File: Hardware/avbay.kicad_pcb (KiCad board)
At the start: 2 copper layers, 45.7 x 95.3 mm, 53 parts, among them P1 TERM_BLOCK_2.54MM_2POS, P2 CONN_6, P3 TERM_BLOCK_2.54MM_8POS, P4 TERM_BLOCK_2.54MM_5POS, P5 TERM_BLOCK_2.54MM_5POS, P6 TERM_BLOCK_2.54MM_2POS, P7 TERM_BLOCK_2.54MM_8POS, Q1 DMN2041LSD, Q2 BSS138DW, Q3 DMN2041LSD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

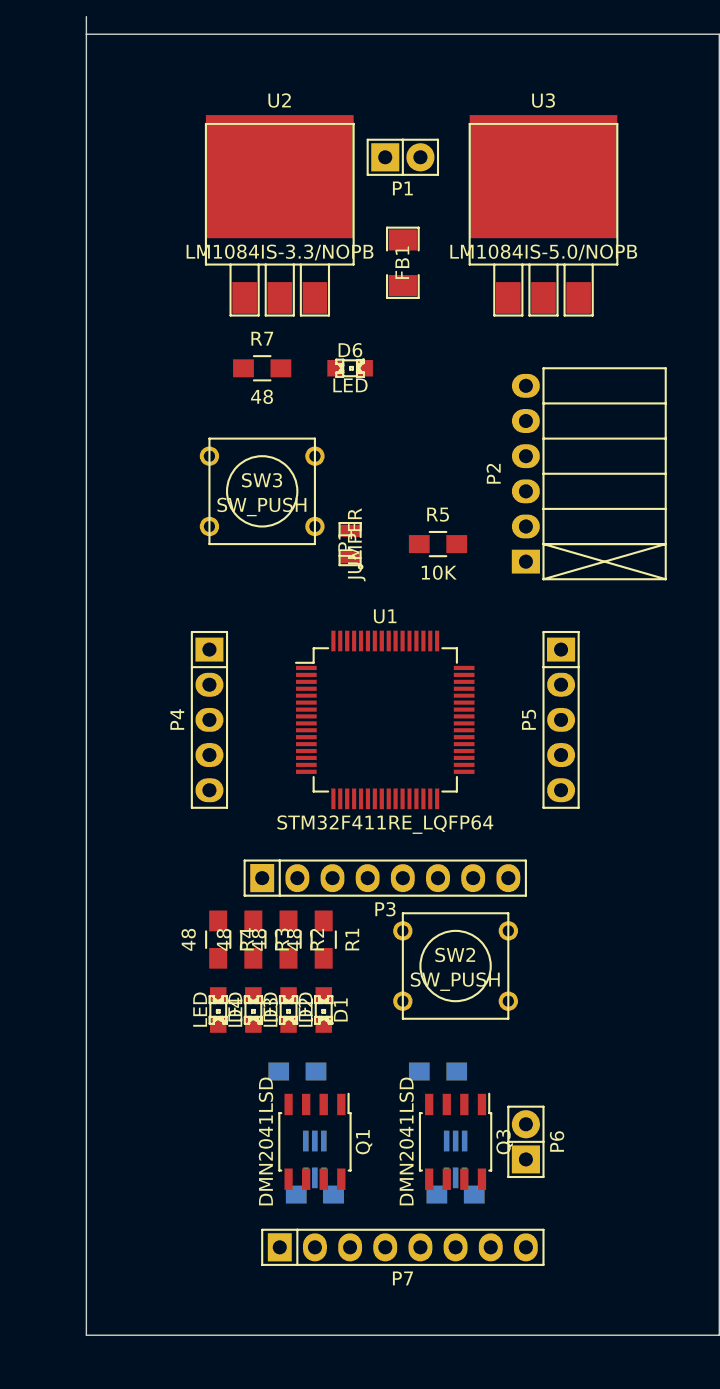
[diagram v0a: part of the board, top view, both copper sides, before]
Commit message: Roughed out PCB layout
Known issues:
- SW_PUSH holes too small. New footprint needed
- Sensor footprints are completely wrong.
- Regulator footprints might not be correct.

Tasks:
- Place passives according to schematic (especially
  with decoupling capacitors.
- Condense layout as much as possible for
  smallest board size
- Route board
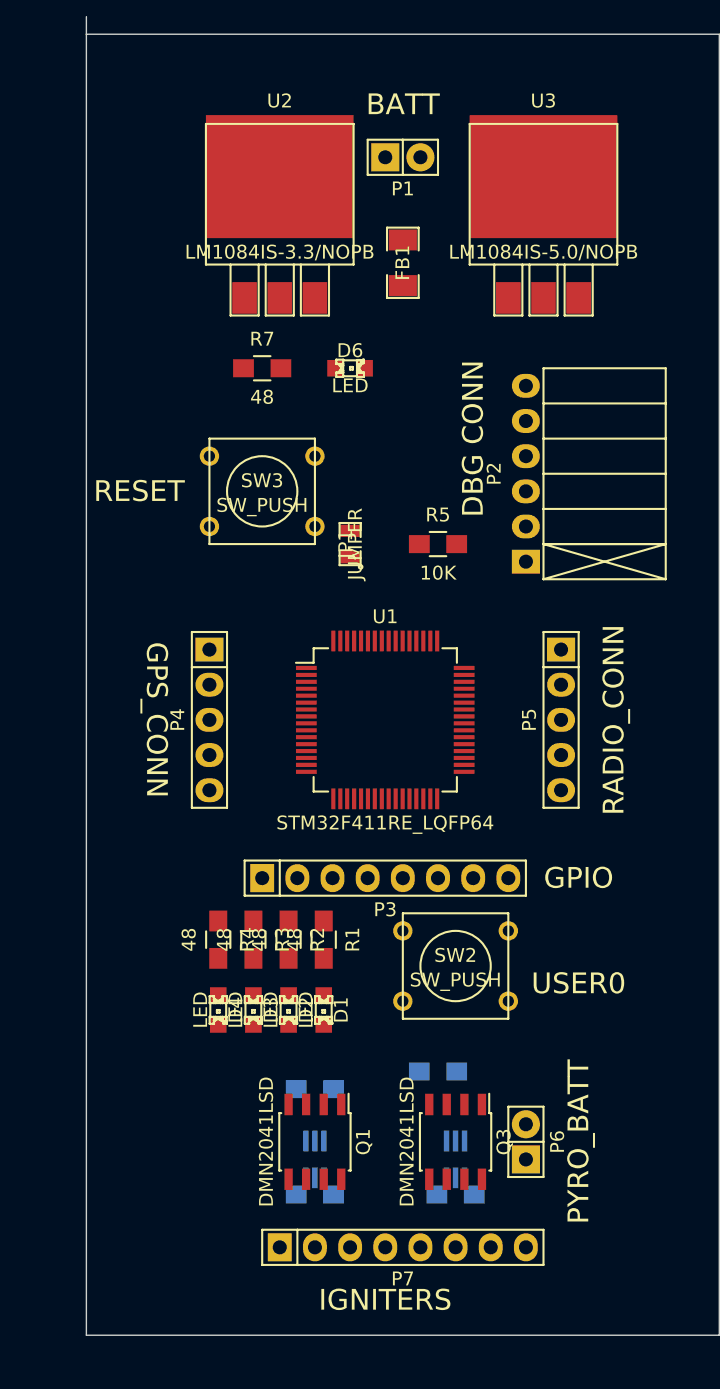
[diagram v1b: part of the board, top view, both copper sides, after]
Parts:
- moved R8 1.80 mm to (147.3, 114.3)
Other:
- board text added: "BATT"
- board text added: "DBG CONN"
- board text added: "GPIO"
- board text added: "GPS_CONN"
- board text added: "IGNITERS"
- board text added: "PYRO_BATT"
- board text added: "RADIO_CONN"
- board text added: "RESET"
- board text added: "USER0"
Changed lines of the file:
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@@
     (area 0 0 0 0)
     (thickness 1.6)
-    (drawings 5)
+    (drawings 14)
     (tracks 0)
     (zones 0)
@@
   )
   (module Resistors_SMD:R_0805_HandSoldering (layer B.Cu)
-    (at 146.05 113.03)
+    (at 147.32 114.3)
     (descr "Resistor SMD 0805, hand soldering")
     (tags "resistor 0805")
@@
     )
   )
+  (gr_text "DBG CONN" (at 158.75 67.31 90) (layer F.SilkS)
+    (effects (font (size 1.5 1.5) (thickness 0.3)))
+  )
+  (gr_text RESET (at 134.62 71.12) (layer F.SilkS)
+    (effects (font (size 1.5 1.5) (thickness 0.3)))
+  )
+  (gr_text BATT (at 153.67 43.18) (layer F.SilkS)
+    (effects (font (size 1.5 1.5) (thickness 0.3)))
+  )
+  (gr_text IGNITERS (at 152.4 129.54) (layer F.SilkS)
+    (effects (font (size 1.5 1.5) (thickness 0.3)))
+  )
+  (gr_text PYRO_BATT (at 166.37 118.11 90) (layer F.SilkS)
+    (effects (font (size 1.5 1.5) (thickness 0.3)))
+  )
+  (gr_text "USER0\n" (at 166.37 106.68) (layer F.SilkS)
+    (effects (font (size 1.5 1.5) (thickness 0.3)))
+  )
+  (gr_text GPIO (at 166.37 99.06) (layer F.SilkS)
+    (effects (font (size 1.5 1.5) (thickness 0.3)))
+  )
+  (gr_text GPS_CONN (at 135.89 87.63 270) (layer F.SilkS)
+    (effects (font (size 1.5 1.5) (thickness 0.3)))
+  )
+  (gr_text "RADIO_CONN\n" (at 168.91 87.63 90) (layer F.SilkS)
+    (effects (font (size 1.5 1.5) (thickness 0.3)))
+  )
   (gr_line (start 130.81 38.1) (end 130.81 36.83) (angle 90) (layer Edge.Cuts) (width 0.1))

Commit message: Began routing
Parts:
- C1, C10, C15, C16, C2, C3, C4, C6, C7, C8, C9, FB1, R6: moved to B.Cu
- U5: footprint Housings_SSOP:SSOP-16_4.4x5.2mm_Pitch0.65mm -> PQFN:PQFN50P300X300-16N-EXTENDED
- U6: footprint Housings_SSOP:SSOP-16_4.4x5.2mm_Pitch0.65mm -> PQFN:PQFN65P400X400-16N-EXTENDED
- moved C12 105.9 mm to (162.6, 62.1), turned to 180 degrees
- moved C16 102.0 mm to (156.2, 69.2)
- moved C13 101.9 mm to (160.0, 60.3), turned to 180 degrees
- moved C4 99.2 mm to (158.1, 60.3), turned to 90 degrees
- moved C15 97.8 mm to (156.2, 77.5)
- moved C3 93.0 mm to (154.9, 57.8), turned to 180 degrees
- moved C8 92.6 mm to (156.8, 93.3), turned to 180 degrees
- moved C14 91.6 mm to (142.2, 60.3), turned to 180 degrees
- moved C5 88.3 mm to (160.0, 95.9), turned to 180 degrees
- moved C9 87.2 mm to (158.1, 83.2), turned to 270 degrees
- moved C2 84.5 mm to (146.1, 63.5), turned to 180 degrees
- moved C11 79.7 mm to (147.3, 60.3)
- moved C7 77.4 mm to (146.1, 67.9)
- moved C1 76.8 mm to (146.1, 60.3), turned to 180 degrees
- moved U5 75.1 mm to (154.9, 61.0), turned to 90 degrees
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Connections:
- C1 pad 1: +3V3 -> 3V3
- FB1 pad 1: +3V3 -> 3V3
- P3 pad 5: +3V3 -> 3V3
- U1 pad 12: /MCU/VDDA -> GND
- U1 pad 13: GND -> /MCU/VDDA
- U1 pad 25: GND -> /MCU/BTN1
- U4 pad 4: +3V3 -> 3V3
- U4 pad 5: +3V3 -> 3V3
- U5 pad 13: +3V3 -> 3V3
- U5 pad 4: +3V3 -> 3V3
- U6 pad 1: +3V3 -> 3V3
- U6 pad 4: +3V3 -> 3V3
- U6 pad 5: +3V3 -> 3V3
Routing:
- net GND: track 0.00 -> 215.6 mm, vias 0 -> 9
- net 3V3: track 0.00 -> 199.1 mm, vias 0 -> 9
- net +5V: track 0.00 -> 95.9 mm
- net /MCU/SENSE1: track 0.00 -> 46.0 mm, vias 0 -> 3
- net /MCU/SENSE2: track 0.00 -> 45.9 mm, vias 0 -> 3
- net /MCU/TRIGGER2: track 0.00 -> 44.9 mm, vias 0 -> 2
- net /Sheet54375BB5/Vbatt: track 0.00 -> 43.3 mm, vias 0 -> 1
- net /MCU/TRIGGER1: track 0.00 -> 41.7 mm, vias 0 -> 2
- net Net-(P7-Pad1): track 0.00 -> 30.8 mm, vias 0 -> 1
- net /MCU/VDDA: track 0.00 -> 27.1 mm, vias 0 -> 3
- net /Pyro/V_PYRO: track 0.00 -> 25.2 mm
- net Net-(P7-Pad7): track 0.00 -> 23.0 mm, vias 0 -> 1
- net Net-(P7-Pad3): track 0.00 -> 23.0 mm
- net /Sensors/SDA: track 0.00 -> 18.0 mm, vias 0 -> 4
- net /MCU/LED0: track 0.00 -> 17.0 mm
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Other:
- net class Default: clearance 0.254 -> 0.1524; trace_width 0.254 -> 0.1524; via_dia 0.889 -> 0.71374; via_drill 0.635 -> 0.3302
- net class Power added: clearance 0.1524, trace_width 0.2032, via_dia 0.71374, via_drill 0.3302
- rule trace_clearance: 0.254 -> 0.1524
- rule trace_min: 0.254 -> 0.1524
- rule via_min_drill: 0.508 -> 0.3302
- rule via_min_size: 0.889 -> 0.71374

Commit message: Finished routing.
Board awaiting review
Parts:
- added 1pin: VAL**, Connect:1pin, F.Cu at (152.4, 53.3)
- P2: footprint Socket_Strips:Socket_Strip_Angled_1x06 -> Socket_Strips:Socket_Strip_Straight_1x06
- moved D6 4.32 mm to (152.4, 49.7)
- moved R7 3.43 mm to (152.4, 48.0)
- moved P2 0.13 mm to (160.5, 71.1)
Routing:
- net GND: track 215.6 -> 349.2 mm, vias 9 -> 18
- net /MCU/NRST: track 0.00 -> 51.9 mm, vias 0 -> 5
- net /MCU/SENSE3: track 0.00 -> 51.7 mm, vias 0 -> 5
- net /MCU/SENSE4: track 0.00 -> 36.6 mm, vias 0 -> 5
- net /MCU/USART_RX: track 0.00 -> 33.4 mm, vias 0 -> 7
- net /MCU/RADIO_RX: track 0.00 -> 32.8 mm, vias 0 -> 6
- net /MCU/TRIGGER4: track 0.00 -> 32.6 mm, vias 0 -> 4
- net /MCU/TRIGGER3: track 0.00 -> 32.5 mm, vias 0 -> 4
- net /MCU/VDDA: track 27.1 -> 56.3 mm, vias 3 -> 6
- net /MCU/JTDO-SWO: track 0.00 -> 25.0 mm, vias 0 -> 2
- net /MCU/RADIO_TX: track 0.00 -> 23.9 mm, vias 0 -> 3
- net /MCU/JTMS-SWDIO: track 0.00 -> 21.1 mm, vias 0 -> 2
- net 3V3: track 199.1 -> 220.0 mm
- net /Sensors/SDA: track 18.0 -> 36.4 mm, vias 4 -> 6
- net /Sensors/SCL: track 15.3 -> 33.1 mm, vias 2 -> 4
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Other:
- board size 45.7 x 95.3 mm -> 30.5 x 81.3 mm
- board text added: "+"
- board text added: "-"
- board text added: "DEBUG"
- board text added: "GPS"
- board text added: "RADIO"
- board text removed: "BATT"
- board text removed: "DBG CONN"
- board text removed: "GPIO"
- board text removed: "GPS_CONN"
- board text removed: "IGNITERS"
- board text removed: "PYRO_BATT"
- board text removed: "RADIO_CONN"
- board text removed: "USER0"

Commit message: Fixed footprints for tecminal blocks
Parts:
- P1, P6: value TERM_BLOCK_2.54MM_2POS -> (none); footprint Socket_Strips:Socket_Strip_Straight_1x02 -> Local:TERM_BLOCK_2
- P3: value TERM_BLOCK_2.54MM_8POS -> (none)
- P4, P5: value TERM_BLOCK_2.54MM_5POS -> (none); footprint Socket_Strips:Socket_Strip_Straight_1x05 -> Local:TERM_BLOCK_5
- P7: value TERM_BLOCK_2.54MM_8POS -> (none); footprint Socket_Strips:Socket_Strip_Straight_1x08 -> Local:TERM_BLOCK_8
- moved P7 8.89 mm to (143.5, 122.6), turned to 0 degrees
- moved P3 8.89 mm to (143.5, 99.1), turned to 0 degrees
- moved P4 5.08 mm to (141.0, 82.5), turned to 270 degrees
- moved P5 5.08 mm to (163.8, 82.5), turned to 270 degrees
- moved P1 1.27 mm to (151.1, 45.7), turned to 0 degrees
- moved P6 1.27 mm to (161.3, 116.8), turned to 90 degrees
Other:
- outline, holes or cut-outs redrawn

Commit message: Finished schematic work. Began footprints
Began assigning footprints for R2
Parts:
- removed 1pin: VAL**, Connect:1pin
- removed C11, C12, C13, C14: 10uF, Capacitors_SMD:C_0805_HandSoldering
- removed C15: .01uF, Capacitors_SMD:C_0805_HandSoldering
- removed C16: .47uF, Capacitors_SMD:C_0805_HandSoldering
- removed C3: .22uF, Capacitors_SMD:C_0805_HandSoldering
- removed C4: 4.6uF, Capacitors_SMD:C_0805_HandSoldering
- removed C7: 100nF, Capacitors_SMD:C_0805_HandSoldering
- removed D6: LED, LEDs:LED-0805
- removed P1: , Local:TERM_BLOCK_2
- removed R6: 10K, Resistors_SMD:R_0805_HandSoldering
- removed R7: 48, Resistors_SMD:R_0805_HandSoldering
- removed SW3: SW_PUSH, Discret:SW_PUSH_SMALL
- removed U2: LM1084IS-3.3/NOPB, SMD_Packages:DPAK-3
- removed U3: LM1084IS-5.0/NOPB, SMD_Packages:DPAK-3
- removed U4: MS5611, SON:SON125P500X300-8N
- removed U5: HMC5883L, PQFN:PQFN50P300X300-16N-EXTENDED
- removed U6: L3G4200D, PQFN:PQFN65P400X400-16N-EXTENDED
- added R12: 10K, Resistors_SMD:R_0805_HandSoldering, F.Cu at (140.2, 111.4)
- added R13: 10K, Resistors_SMD:R_0805_HandSoldering, F.Cu at (140.2, 113.9)
- added R14, R15: 10K, Resistors_SMD:R_0805_HandSoldering, F.Cu at (152.4, 134.5)
- P3, P7: value (none) -> TERM_BLOCK_2.54MM_8POS
- P4, P5: value (none) -> TERM_BLOCK_2.54MM_5POS
- P6: value (none) -> TERM_BLOCK_2.54MM_2POS
- moved P2 2.39 mm to (162.8, 70.4)
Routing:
- net GND: track 349.2 -> 229.8 mm, vias 18 -> 13
- net 3V3: track 220.0 -> 149.9 mm
- net /MCU/NRST: track 51.9 -> 0.00 mm, vias 5 -> 0
- net /Sheet54375BB5/Vbatt: track 44.9 -> 0.00 mm, vias 2 -> 0
- net +5V: track 96.5 -> 55.0 mm
- net /MCU/VDDA: track 56.3 -> 19.5 mm, vias 6 -> 3
- net /Sensors/SDA: track 36.4 -> 0.00 mm, vias 6 -> 0
- net /Sensors/SCL: track 33.1 -> 0.00 mm, vias 4 -> 0
- net /MCU/JTDO-SWO: track 25.0 -> 0.00 mm, vias 2 -> 0
- net /MCU/JTMS-SWDIO: track 21.1 -> 0.00 mm, vias 2 -> 0
- net Net-(C15-Pad1): track 14.1 -> 0.00 mm, vias 2 -> 0
- net /MCU/JTCK-SWCLK: track 9.16 -> 0.00 mm, vias 2 -> 0
- net /MCU/TRIGGER1: track 42.1 -> 35.7 mm, vias 2 -> 1
- net Net-(C3-Pad1): track 6.21 -> 0.00 mm, vias 2 -> 0
- net Net-(C16-Pad2): track 6.08 -> 0.00 mm
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
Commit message: Ready to begin laying out and routing
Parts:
- added ?: , Local:MOUNTING_HOLE_3mm, F.Cu at (139.4, 122.2)
- added ?: , Local:MOUNTING_HOLE_3mm, F.Cu at (165.4, 45.5)
- added C11: 10uF, Capacitors_SMD:C_0805_HandSoldering, F.Cu at (192.1, 127.3)
- added C12: .01uF, Capacitors_SMD:C_0805_HandSoldering, F.Cu at (199.8, 130.8)
- added C13: 100uF, Local:SMD_CAP, F.Cu at (200.0, 143.7)
- added C14: 10uF, Capacitors_SMD:C_0805_HandSoldering, F.Cu at (200.7, 124.7)
- added C3: 10uF, Capacitors_SMD:C_0805_HandSoldering, F.Cu at (124.1, 137.9)
- added C4: 3.3nF, Capacitors_SMD:C_0805_HandSoldering, F.Cu at (140.3, 136.6)
- added C7: 100nF, Capacitors_SMD:C_0805_HandSoldering, F.Cu at (140.7, 142.6)
- added D5: DIODE, Diodes_SMD:Diode-MELF_Handsoldering, F.Cu at (170.9, 137.6)
- added D6: LED, LEDs:LED-0805, F.Cu at (217.0, 130.1)
- added D7: DIODESCH, Diodes_SMD:Diode-MELF_Handsoldering, F.Cu at (180.6, 145.5)
- added D8: DIODE, Diodes_SMD:Diode-MELF_Handsoldering, F.Cu at (186.7, 136.0)
- added L1: 20uH, Capacitors_SMD:C_2220_HandSoldering, F.Cu at (164.1, 145.5)
- added P1: TERM_BLOCK_2.54MM_2POS, Local:TERM_BLOCK_2, F.Cu at (189.2, 117.3)
- added P8: CONN_01X02, Socket_Strips:Socket_Strip_Straight_2x01, F.Cu at (172.4, 115.3)
- added Q5: NPN, Housings_SOT-23_SOT-143_TSOT-6:SOT-23_Handsoldering, F.Cu at (210.3, 136.3)
- added R16: 180, Resistors_SMD:R_0805_HandSoldering, F.Cu at (140.1, 130.6)
- added R7: 48, Resistors_SMD:R_0805_HandSoldering, F.Cu at (202.6, 118.2)
- added SP1: SPEAKER, Local:CBT-07427, F.Cu at (178.6, 126.0)
- added SW3: SW_PUSH, Local:SW_SMD_MICRO, F.Cu at (209.0, 126.0)
- added U2: MIC5209-3.3, SMD_Packages:SOT-223, F.Cu at (130.6, 141.0)
- added U3: LT1376IS8-5, Housings_SOIC:SOIC-8_3.9x4.9mm_Pitch1.27mm, F.Cu at (146.9, 152.9)
- added U4: MS5611, Local:MS5611-EXT, F.Cu at (136.1, 153.4)
- added U5: ADXL375, Local:ADXL375-EXT, F.Cu at (127.1, 153.2)
- SW2: footprint Discret:SW_PUSH_SMALL -> Local:SW_SMD
- moved R14 25.5 mm to (126.9, 133.4)
- moved R15 19.4 mm to (133.0, 134.0)
- moved C2 16.0 mm to (153.5, 77.7), turned to 90 degrees
- moved C1 13.4 mm to (148.7, 73.4)
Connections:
- U1 pad 58: /MCU/GPIO6 -> /Sensors/ACCEL_INT_1
- U1 pad 59: /MCU/GPIO7 -> /Sensors/ACCEL_INT_2
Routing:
- net 3V3: track 149.9 -> 130.2 mm, vias 9 -> 7
- net GND: track 229.8 -> 215.3 mm
- net /MCU/BTN0: track 22.9 -> 15.2 mm
- net (no net): track 1.81 -> 7.62 mm
- net /MCU/USART_RX: track 33.4 -> 34.4 mm, vias 7 -> 5
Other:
- outline, holes or cut-outs redrawn

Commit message: Began routing
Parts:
- C12, C4, D5, Q5, R16, U5: moved to B.Cu
- moved C13 107.8 mm to (151.1, 47.6)
- moved U3 105.9 mm to (158.1, 47.6), turned to 90 degrees
- moved C3 96.5 mm to (164.5, 50.2)
- moved D7 96.0 mm to (151.8, 54.0)
- moved U4 92.4 mm to (157.5, 63.5)
- moved Q5 92.0 mm to (147.3, 69.2)
- moved C4 90.7 mm to (158.1, 47.6)
- moved L1 90.3 mm to (162.6, 55.2)
- moved D6 90.1 mm to (152.4, 67.3)
- moved U5 88.1 mm to (157.5, 70.5), turned to 90 degrees
- moved C12 85.7 mm to (159.4, 55.2), turned to 90 degrees
- moved D8 85.7 mm to (151.8, 57.8)
- moved P1 85.2 mm to (141.3, 46.9)
- moved U2 84.7 mm to (142.2, 57.1)
- moved C14 82.9 mm to (144.8, 63.5)
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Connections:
- C11 pad 1: /Sheet54375BB5/Vbatt -> +5V
- U2 pad 1: /Sheet54375BB5/Vbatt -> +5V
- U2 pad 3: (no net) -> 3V3
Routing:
- net GND: track 215.3 -> 346.9 mm, vias 13 -> 26
- net +5V: track 55.0 -> 137.5 mm
- net /MCU/NRST: track 0.00 -> 74.5 mm, vias 0 -> 2
- net 3V3: track 130.2 -> 190.8 mm, vias 7 -> 11
- net /MCU/VDDA: track 19.5 -> 63.8 mm, vias 3 -> 8
- net /Sensors/SDA: track 0.00 -> 37.7 mm, vias 0 -> 2
- net /Sheet54375BB5/Vbatt: track 0.00 -> 36.0 mm
- net /Sensors/SCL: track 0.00 -> 34.5 mm, vias 0 -> 2
- net /MCU/GPIO4: track 0.00 -> 21.9 mm, vias 0 -> 3
- net Net-(C12-Pad1): track 0.00 -> 15.8 mm, vias 0 -> 1
- net Net-(D5-Pad1): track 0.00 -> 13.7 mm, vias 0 -> 2
- net Net-(C12-Pad2): track 0.00 -> 12.4 mm, vias 0 -> 1
- net (no net): track 7.62 -> 0.92 mm
- net /MCU/SENSE3: track 51.7 -> 56.1 mm
- net Net-(C4-Pad1): track 0.00 -> 2.97 mm, vias 0 -> 1
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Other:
- board size 30.5 x 81.3 mm -> 30.5 x 83.2 mm

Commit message: Routed more stuff
Almost all routing is done, except for the accelerometer interrupt lines
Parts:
- moved ? 1.94 mm to (139.4, 124.1)
- turned R15 to 90 degrees
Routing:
- net GND: track 346.9 -> 396.4 mm
- net /MCU/JTDO-SWO: track 0.00 -> 31.1 mm, vias 0 -> 2
- net /MCU/JTMS-SWDIO: track 0.00 -> 23.2 mm, vias 0 -> 2
- net 3V3: track 190.8 -> 210.5 mm
- net /MCU/JTCK-SWCLK: track 0.00 -> 17.4 mm, vias 0 -> 2
- net +5V: track 137.5 -> 147.2 mm, vias 0 -> 2
- net /MCU/TRIGGER2: track 43.5 -> 52.7 mm, vias 1 -> 2
- net /MCU/TRIGGER1: track 35.7 -> 43.2 mm, vias 1 -> 2
- net /MCU/SENSE2: track 43.0 -> 49.8 mm, vias 2 -> 3
- net /MCU/SENSE1: track 43.7 -> 50.4 mm, vias 2 -> 3
- net /MCU/TRIGGER3: track 32.5 -> 37.4 mm
- net /MCU/TRIGGER4: track 32.6 -> 34.6 mm
- net /MCU/RADIO_RX: track 32.8 -> 34.3 mm
- net /MCU/VDDA: track 63.8 -> 62.5 mm
